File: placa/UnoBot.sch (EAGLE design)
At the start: 36 parts, among them U1 GY-521MPU6050

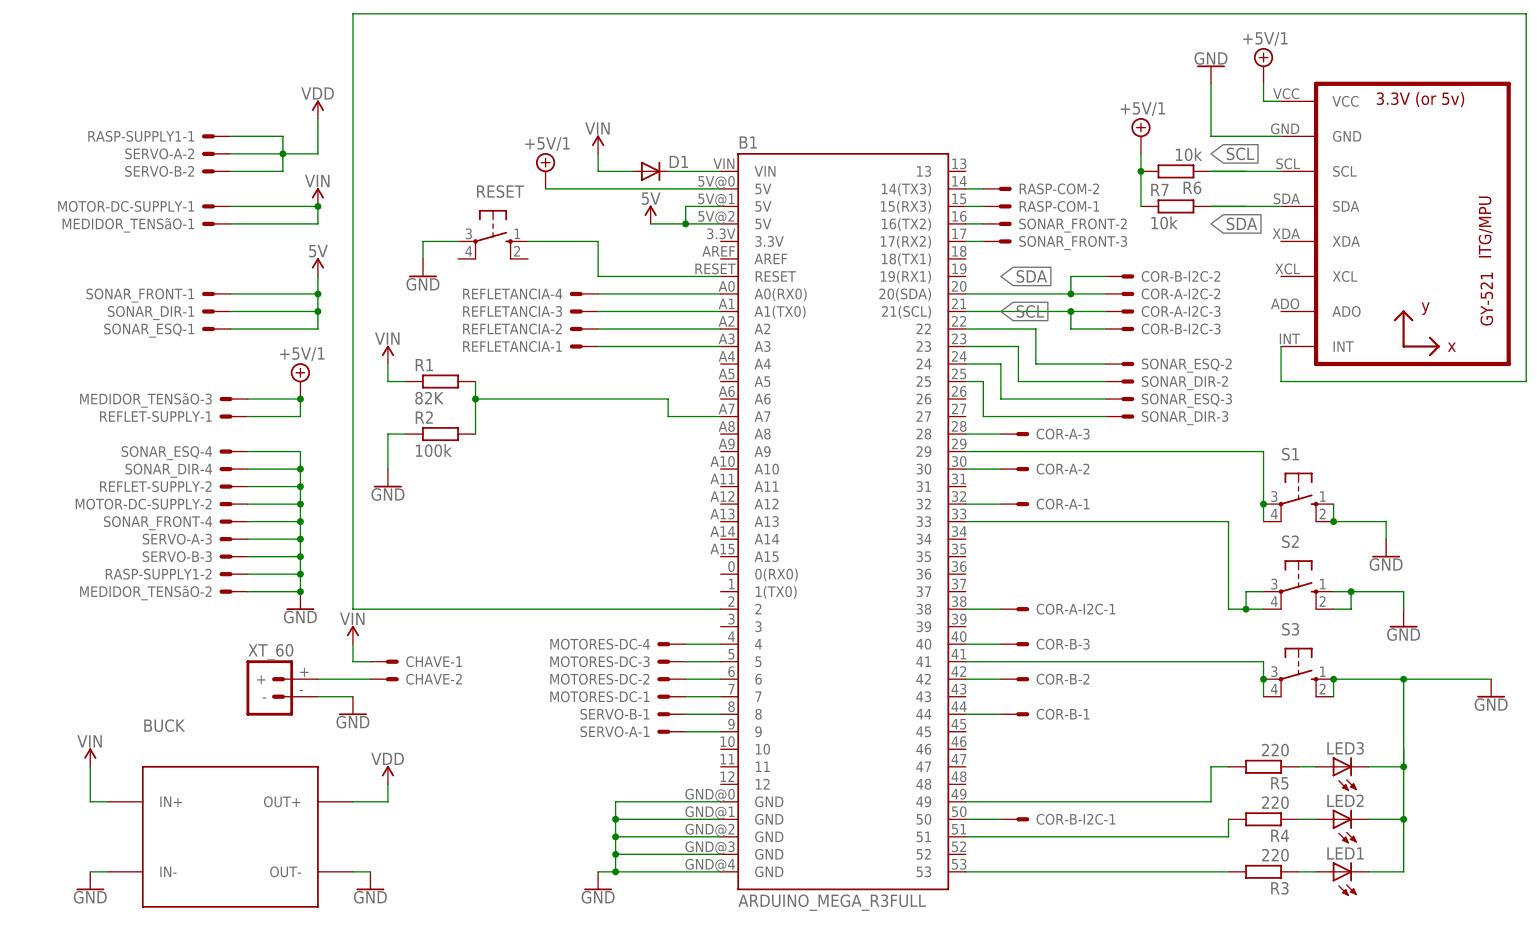
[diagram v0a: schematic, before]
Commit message: Adição da versão mais atualizada da placa Unobot
foi adiciona dos arquivos da placa shild unobot
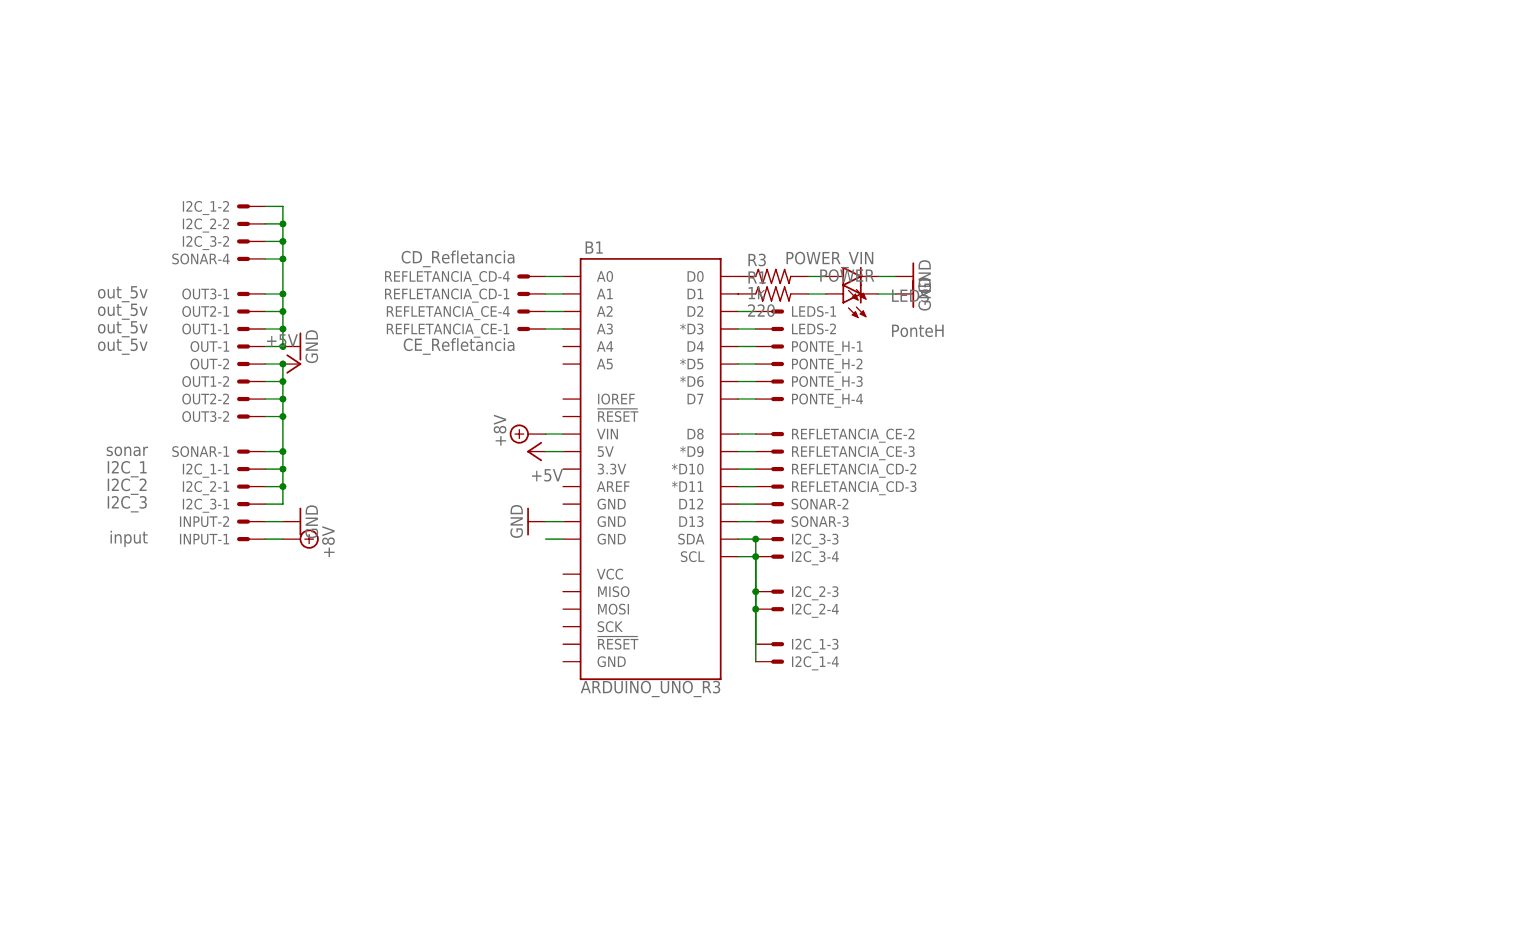
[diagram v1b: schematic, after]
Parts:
- removed BUCK: DC-DC-STEP-DOWN-LM2596, 1484249208697-powermodules:DC-DC-STEP-DOWN-LM2596
- removed CHAVE, MOTOR-DC-SUPPLY, RASP-COM, RASP-SUPPLY1, REFLET-SUPPLY: 22-23-2021, con-molex:22-23-2021
- removed COR-A, COR-A-I2C, COR-B, COR-B-I2C, MEDIDOR_TENSãO, SERVO-A, SERVO-B: 22-23-2031, con-molex:22-23-2031
- removed D1: 1N4004, diode:1N4004
- removed LED1, LED2, LED3: (no value), led:LED5MM
- removed MOTORES-DC, REFLETANCIA, SONAR_DIR, SONAR_ESQ, SONAR_FRONT: 22-23-2041, con-molex:22-23-2041
- removed R2: 100k, rcl:R-EU_0207/12
- removed R4, R5: 220, rcl:R-EU_0207/7
- removed R6, R7: 10k, rcl:R-EU_0204/7
- removed RESET, S1, S2, S3: (no value), switch-omron:10-XX
- removed U1: GY-521MPU6050, gy-521:GY-521MPU6050
- removed XT_60: (no value), Robotica-IFRN-SC-conectores:BATTERY_CONNXT60
- added I2C_1: I2C_1, Rembrandt Electronics - JST XH Connectors v1-0:JST-XH-04-PIN-LONG-PAD
- added I2C_2: I2C_2, Rembrandt Electronics - JST XH Connectors v1-0:JST-XH-04-PIN-LONG-PAD
- added I2C_3: I2C_3, Rembrandt Electronics - JST XH Connectors v1-0:JST-XH-04-PIN-LONG-PAD
- added INPUT: input, Rembrandt Electronics - JST XH Connectors v1-0:JST-XH-02-PIN-LONG-PAD
- added LEDS: LEDS, Rembrandt Electronics - JST XH Connectors v1-0:JST-XH-02-PIN-LONG-PAD
- added OUT, OUT1, OUT2, OUT3: out_5v, Rembrandt Electronics - JST XH Connectors v1-0:JST-XH-02-PIN-LONG-PAD
- added PONTE_H: PonteH, Rembrandt Electronics - JST XH Connectors v1-0:JST-XH-04-PIN-LONG-PAD
- added POWER, POWER_VIN: (no value), led_robotica:LEDLED5MM_LONG_PAD
- added REFLETANCIA_CD: CD_Refletancia, Rembrandt Electronics - JST XH Connectors v1-0:JST-XH-04-PIN-LONG-PAD
- added REFLETANCIA_CE: CE_Refletancia, Rembrandt Electronics - JST XH Connectors v1-0:JST-XH-04-PIN-LONG-PAD
- added SONAR: sonar, Rembrandt Electronics - JST XH Connectors v1-0:JST-XH-04-PIN-LONG-PAD
- B1: value ARDUINO_MEGA_R3FULL -> ARDUINO_UNO_R3; device SparkFun-Boards3:ARDUINO_MEGA_R3FULL -> SparkFun-Boards:ARDUINO_UNO_R3
- R1: value 82K -> 220; device rcl:R-EU_0207/12 -> rcl_robotica:R-US_0204/7
- R3: value 220 -> 1k; device rcl:R-EU_0207/7 -> rcl_robotica:R-US_0204/7
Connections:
- removed net +5V/1: B1.5V@0, MEDIDOR_TENSãO-3.S, R6.2, R7.1, REFLET-SUPPLY-1.S, U1.VCC
- removed net 5V: B1.5V@1, B1.5V@2, SONAR_DIR-1.S, SONAR_ESQ-1.S, SONAR_FRONT-1.S
- removed net N$22: B1.51, R4.2
- removed net N$23: B1.49, R5.2
- removed net N$24: LED3.A, R5.1
- removed net N$25: LED2.A, R4.1
- removed net N$26: LED1.A, R3.1
- removed net N$27: B1.33, S2.P, S2.P1
- removed net N$28: B1.29, S1.P, S1.P1
- removed net N$30: B1.41, S3.P, S3.P1
- removed net N$31: B1.RESET, RESET.S
- removed net N$33: B1.A0(RX0), REFLETANCIA-4.S
- removed net N$34: B1.25, SONAR_DIR-3.S
- removed net N$35: B1.24, SONAR_ESQ-3.S
- removed net N$36: B1.23, SONAR_DIR-2.S
- removed net N$37: B1.22, SONAR_ESQ-2.S
- removed net N$39: B1.2, U1.INT
- removed net N$40: B1.50, COR-B-I2C-1.S
- removed net N$41: B1.28, COR-A-3.S
- removed net SCL: B1.21(SCL), COR-A-I2C-3.S, COR-B-I2C-3.S, R6.1, U1.SCL
- removed net SDA: B1.20(SDA), COR-A-I2C-2.S, COR-B-I2C-2.S, R7.2, U1.SDA
- removed net VDD: BUCK.OUT+, RASP-SUPPLY1-1.S, SERVO-A-2.S, SERVO-B-2.S
- removed net VIN: BUCK.IN+, CHAVE-1.S, D1.A, MEDIDOR_TENSãO-1.S, MOTOR-DC-SUPPLY-1.S, R1.1
- new net +5V: B1.5V, I2C_1-1.S, I2C_2-1.S, I2C_3-1.S, OUT-2.S, OUT1-2.S, OUT2-2.S, OUT3-2.S, SONAR-1.S
- new net +8V: B1.VIN, INPUT-1.S
- net GND: now also I2C_1-2.S, I2C_2-2.S, I2C_3-2.S, INPUT-2.S, OUT-1.S, OUT1-1.S, OUT2-1.S, OUT3-1.S, POWER.C, POWER_VIN.C, SONAR-4.S; no longer B1.GND@0, B1.GND@2, B1.GND@3, B1.GND@4, BUCK.IN-, BUCK.OUT-, LED1.C, LED2.C, LED3.C, MEDIDOR_TENSãO-2.S, MOTOR-DC-SUPPLY-2.S, R2.1, RASP-SUPPLY1-2.S, REFLET-SUPPLY-2.S, RESET.P, S1.S, S1.S1, S2.S, S2.S1, S3.S, S3.S1, SERVO-A-3.S, SERVO-B-3.S, SONAR_DIR-4.S, SONAR_ESQ-4.S, SONAR_FRONT-4.S, U1.GND, XT_60.-
- net N$1: now also B1.D4, PONTE_H-1.S; no longer B1.A2, REFLETANCIA-2.S
- net N$10: now also B1.*D9, REFLETANCIA_CE-3.S; no longer B1.15(RX3), RASP-COM-1.S
- net N$11: now also B1.*D10, REFLETANCIA_CD-2.S; no longer B1.16(TX2), SONAR_FRONT-2.S
- net N$12: now also B1.*D11, REFLETANCIA_CD-3.S; no longer B1.17(RX2), SONAR_FRONT-3.S
- net N$13: now also B1.D13, SONAR-3.S; no longer CHAVE-2.S, XT_60.+
- net N$14: now also B1.SDA, I2C_1-3.S, I2C_2-3.S, I2C_3-3.S; no longer B1.32, COR-A-1.S
- net N$15: now also B1.D12, SONAR-2.S; no longer B1.30, COR-A-2.S
- net N$16: now also B1.SCL, I2C_1-4.S, I2C_2-4.S, I2C_3-4.S; no longer B1.38, COR-A-I2C-1.S
- net N$17: now also B1.GND@0; no longer B1.40, COR-B-3.S
- net N$18: now also B1.D2, LEDS-1.S; no longer B1.42, COR-B-2.S
- net N$19: now also B1.*D3, LEDS-2.S; no longer B1.44, COR-B-1.S
- net N$2: now also B1.*D5, PONTE_H-2.S; no longer B1.A3, REFLETANCIA-1.S
- net N$20: now also B1.D1, R1.1; no longer B1.A7, R1.2, R2.2
- net N$21: now also B1.D0, R3.1; no longer B1.53, R3.2
- net N$29: now also POWER_VIN.A, R3.2; no longer B1.A1(TX0), REFLETANCIA-3.S
- net N$3: now also B1.*D6, PONTE_H-3.S; no longer B1.4, MOTORES-DC-4.S
- net N$32: now also POWER.A, R1.2; no longer B1.VIN, D1.C
- net N$4: now also B1.D7, PONTE_H-4.S; no longer B1.5, MOTORES-DC-3.S
- net N$5: now also B1.A0, REFLETANCIA_CD-4.S; no longer B1.6, MOTORES-DC-2.S
- net N$6: now also B1.A1, REFLETANCIA_CD-1.S; no longer B1.7, MOTORES-DC-1.S
- net N$7: now also B1.A2, REFLETANCIA_CE-4.S; no longer B1.8, SERVO-B-1.S
- net N$8: now also B1.A3, REFLETANCIA_CE-1.S; no longer B1.9, SERVO-A-1.S
- net N$9: now also B1.D8, REFLETANCIA_CE-2.S; no longer B1.14(TX3), RASP-COM-2.S
